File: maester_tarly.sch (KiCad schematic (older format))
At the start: 30 parts, among them J101 Micro_SD_Card_Det, J102 USB_B_Micro, J103 USB_A, J104 Conn_01x06, J105 Conn_01x10, J106 RJ45_Amphenol_RJMG1BD3B8K1ANR, J107 DF40GB(1.5)-48DS-0.4V, J108 DF40GB(1.5)-48DS-0.4V, J109 DF40GB(1.5)-48DS-0.4V, J110 DF40GB(1.5)-48DS-0.4V

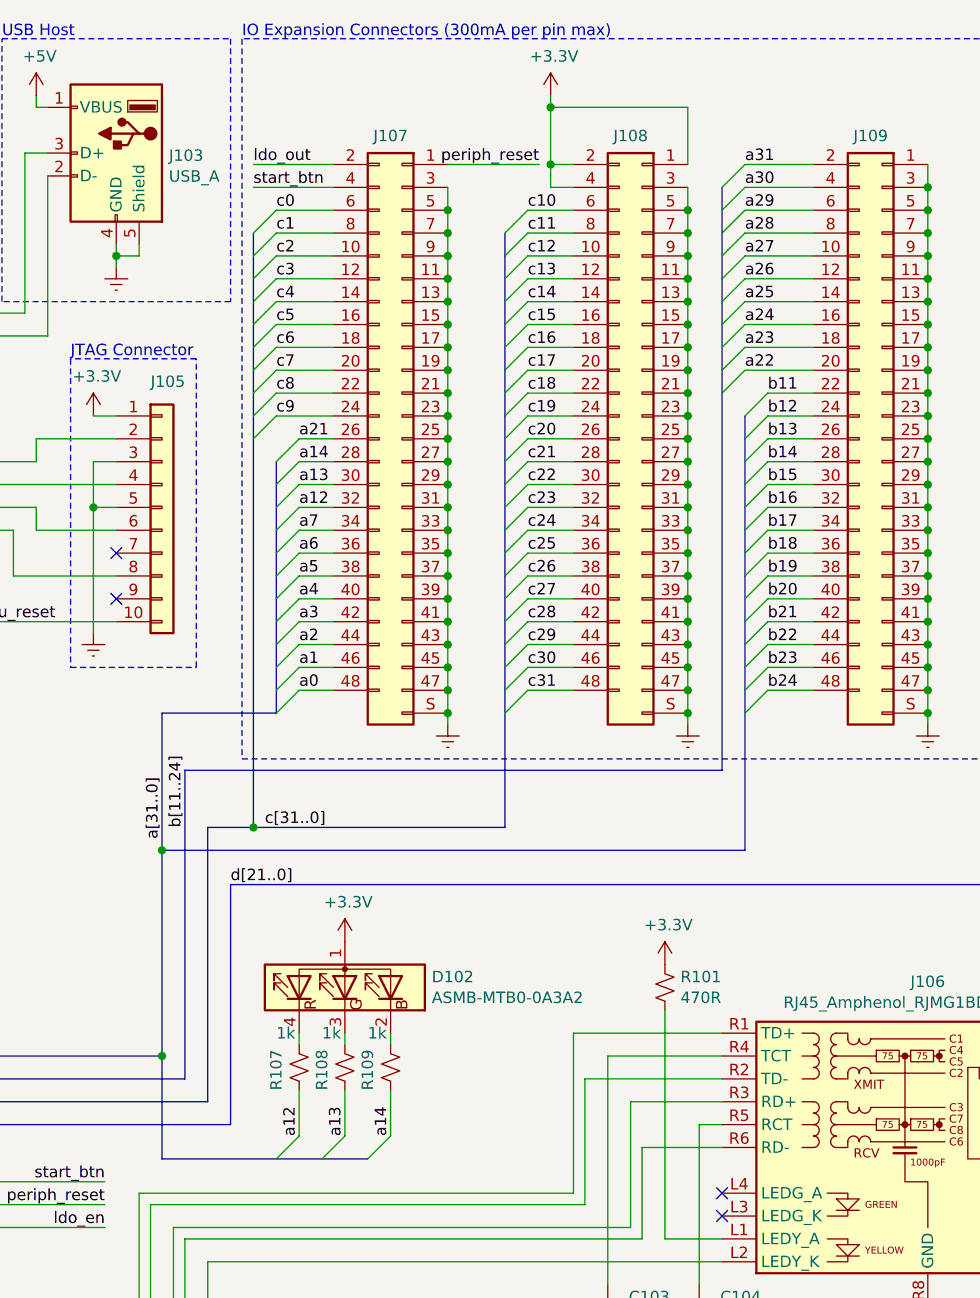
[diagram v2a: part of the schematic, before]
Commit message: Wired up J107 and J109
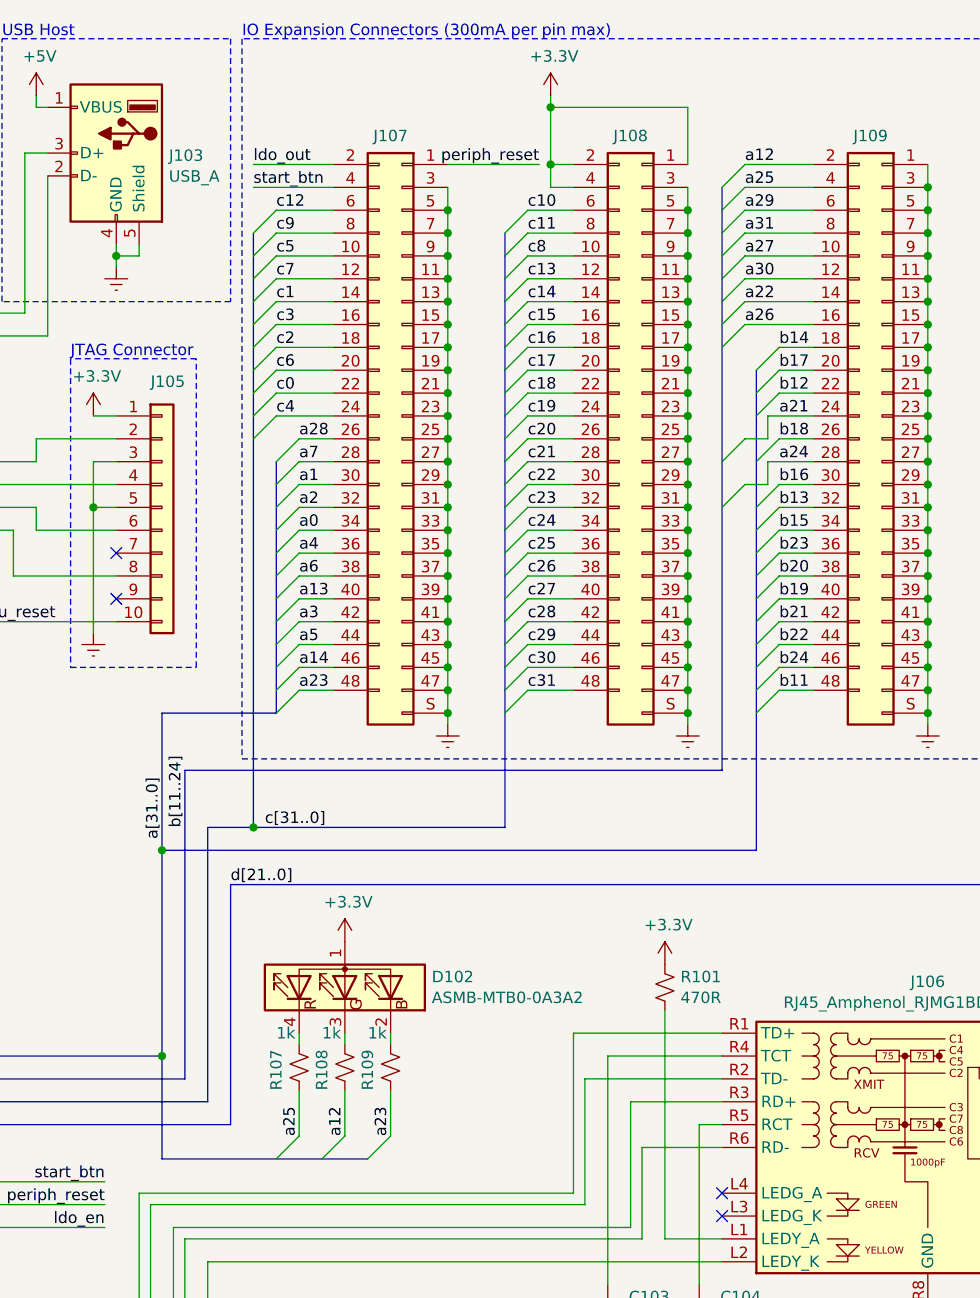
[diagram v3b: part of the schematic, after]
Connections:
- net a0: now also J107.34 (Pin_34); no longer J107.48 (Pin_48)
- net a1: now also J107.30 (Pin_30); no longer J107.46 (Pin_46)
- net a12: now also J109.2 (Pin_2), R108.2; no longer J107.32 (Pin_32), R107.2
- net a13: now also J107.40 (Pin_40); no longer J107.30 (Pin_30), R108.2
- net a14: now also J107.46 (Pin_46); no longer J107.28 (Pin_28), R109.2
- net a2: now also J107.32 (Pin_32); no longer J107.44 (Pin_44)
- net a21: now also J109.24 (Pin_24); no longer J107.26 (Pin_26)
- net a22: now also J109.14 (Pin_14); no longer J109.20 (Pin_20)
- net a23: now also J107.48 (Pin_48), R109.2; no longer J109.18 (Pin_18)
- net a24: now also J109.28 (Pin_28); no longer J109.16 (Pin_16)
- net a25: now also J109.4 (Pin_4), R107.2; no longer J109.14 (Pin_14)
- net a26: now also J109.16 (Pin_16); no longer J109.12 (Pin_12)
- net a28: now also J107.26 (Pin_26); no longer J109.8 (Pin_8)
- net a30: now also J109.12 (Pin_12); no longer J109.4 (Pin_4)
- net a31: now also J109.8 (Pin_8); no longer J109.2 (Pin_2)
- net a4: now also J107.36 (Pin_36); no longer J107.40 (Pin_40)
- net a5: now also J107.44 (Pin_44); no longer J107.38 (Pin_38)
- net a6: now also J107.38 (Pin_38); no longer J107.36 (Pin_36)
- net a7: now also J107.28 (Pin_28); no longer J107.34 (Pin_34)
- net b11: now also J109.48 (Pin_48); no longer J109.22 (Pin_22)
- net b12: now also J109.22 (Pin_22); no longer J109.24 (Pin_24)
- net b13: now also J109.32 (Pin_32); no longer J109.26 (Pin_26)
- net b14: now also J109.18 (Pin_18); no longer J109.28 (Pin_28)
- net b15: now also J109.34 (Pin_34); no longer J109.30 (Pin_30)
- net b16: now also J109.30 (Pin_30); no longer J109.32 (Pin_32)
- net b17: now also J109.20 (Pin_20); no longer J109.34 (Pin_34)
- net b18: now also J109.26 (Pin_26); no longer J109.36 (Pin_36)
- net b19: now also J109.40 (Pin_40); no longer J109.38 (Pin_38)
- net b20: now also J109.38 (Pin_38); no longer J109.40 (Pin_40)
- net b23: now also J109.36 (Pin_36); no longer J109.46 (Pin_46)
- net b24: now also J109.46 (Pin_46); no longer J109.48 (Pin_48)
- net c0: now also J107.22 (Pin_22); no longer J107.6 (Pin_6)
- net c1: now also J107.14 (Pin_14); no longer J107.8 (Pin_8)
- net c12: now also J107.6 (Pin_6); no longer J108.10 (Pin_10)
- net c2: now also J107.18 (Pin_18); no longer J107.10 (Pin_10)
- net c3: now also J107.16 (Pin_16); no longer J107.12 (Pin_12)
- net c4: now also J107.24 (Pin_24); no longer J107.14 (Pin_14)
- net c5: now also J107.10 (Pin_10); no longer J107.16 (Pin_16)
- net c6: now also J107.20 (Pin_20); no longer J107.18 (Pin_18)
- net c7: now also J107.12 (Pin_12); no longer J107.20 (Pin_20)
- net c8: now also J108.10 (Pin_10); no longer J107.22 (Pin_22)
- net c9: now also J107.8 (Pin_8); no longer J107.24 (Pin_24)

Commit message: 27 Unrouted traces remaiin.
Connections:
- net c10: now also J108.36 (Pin_36); no longer J108.6 (Pin_6)
- net c11: now also J108.48 (Pin_48); no longer J108.8 (Pin_8)
- net c13: now also J108.30 (Pin_30); no longer J108.12 (Pin_12)
- net c14: now also J108.46 (Pin_46); no longer J108.14 (Pin_14)
- net c15: now also J108.34 (Pin_34); no longer J108.16 (Pin_16)
- net c16: now also J108.44 (Pin_44); no longer J108.18 (Pin_18)
- net c17: now also J108.18 (Pin_18); no longer J108.20 (Pin_20)
- net c18: now also J108.42 (Pin_42); no longer J108.22 (Pin_22)
- net c19: now also J108.28 (Pin_28); no longer J108.24 (Pin_24)
- net c20: now also J108.24 (Pin_24); no longer J108.26 (Pin_26)
- net c21: now also J108.20 (Pin_20); no longer J108.28 (Pin_28)
- net c22: now also J108.38 (Pin_38); no longer J108.30 (Pin_30)
- net c23: now also J108.10 (Pin_10); no longer J108.32 (Pin_32)
- net c24: now also J108.32 (Pin_32); no longer J108.34 (Pin_34)
- net c25: now also J108.14 (Pin_14); no longer J108.36 (Pin_36)
- net c26: now also J108.26 (Pin_26); no longer J108.38 (Pin_38)
- net c27: now also J108.16 (Pin_16); no longer J108.40 (Pin_40)
- net c28: now also J108.12 (Pin_12); no longer J108.42 (Pin_42)
- net c29: now also J108.8 (Pin_8); no longer J108.44 (Pin_44)
- net c30: now also J108.40 (Pin_40); no longer J108.46 (Pin_46)
- net c31: now also J108.6 (Pin_6); no longer J108.48 (Pin_48)
- net c8: now also J108.22 (Pin_22); no longer J108.10 (Pin_10)
- net d0: now also J110.48 (Pin_48); no longer J110.6 (Pin_6)
- net d1: now also J110.46 (Pin_46); no longer J110.8 (Pin_8)
- net d10: now also J110.24 (Pin_24); no longer J110.26 (Pin_26)
- net d11: now also J110.10 (Pin_10); no longer J110.28 (Pin_28)
- net d12: now also J110.26 (Pin_26); no longer J110.30 (Pin_30)
- net d13: now also J110.22 (Pin_22); no longer J110.32 (Pin_32)
- net d14: now also J110.12 (Pin_12); no longer J110.34 (Pin_34)
- net d15: now also J110.30 (Pin_30); no longer J110.36 (Pin_36)
- net d16: now also J110.44 (Pin_44); no longer J110.38 (Pin_38)
- net d17: now also J110.34 (Pin_34); no longer J110.40 (Pin_40)
- net d18: now also J110.8 (Pin_8); no longer J110.42 (Pin_42)
- net d19: now also J110.38 (Pin_38); no longer J110.44 (Pin_44)
- net d2: now also J110.40 (Pin_40); no longer J110.10 (Pin_10)
- net d20: now also J110.14 (Pin_14); no longer J110.46 (Pin_46)
- net d21: now also J110.32 (Pin_32); no longer J110.48 (Pin_48)
- net d3: now also J110.36 (Pin_36); no longer J110.12 (Pin_12)
- net d4: now also J110.42 (Pin_42); no longer J110.14 (Pin_14)
- net d7: now also J110.28 (Pin_28); no longer J110.20 (Pin_20)
- net d8: now also J110.20 (Pin_20); no longer J110.22 (Pin_22)
- net d9: now also J110.6 (Pin_6); no longer J110.24 (Pin_24)
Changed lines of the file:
@@
 Text Label 7200 1700 0    50   ~ 0
 c7
-Text Label 8300 1600 0    50   ~ 0
+Text Label 8300 2200 0    50   ~ 0
 c8
 Text Label 7200 1500 0    50   ~ 0
 c9
-Text Label 8300 1400 0    50   ~ 0
+Text Label 8300 2900 0    50   ~ 0
 c10
-Text Label 8300 1500 0    50   ~ 0
+Text Label 8300 3500 0    50   ~ 0
 c11
 Text Label 7200 1400 0    50   ~ 0
 c12
-Text Label 8300 1700 0    50   ~ 0
+Text Label 8300 2600 0    50   ~ 0
 c13
-Text Label 8300 1800 0    50   ~ 0
+Text Label 8300 3400 0    50   ~ 0
 c14
-Text Label 8300 1900 0    50   ~ 0
+Text Label 8300 2800 0    50   ~ 0
 c15
+Text Label 8300 3300 0    50   ~ 0
+c16
 Text Label 8300 2000 0    50   ~ 0
-c16
+c17
+Text Label 8300 3200 0    50   ~ 0
+c18
+Text Label 8300 2500 0    50   ~ 0
+c19
+Text Label 8300 2300 0    50   ~ 0
+c20
 Text Label 8300 2100 0    50   ~ 0
-c17
-Text Label 8300 2200 0    50   ~ 0
-c18
-Text Label 8300 2300 0    50   ~ 0
-c19
-Text Label 8300 2400 0    50   ~ 0
-c20
-Text Label 8300 2500 0    50   ~ 0
 c21
 Wire Wire Line
@@
 Wire Wire Line
 	1250 2300 4250 2300
-Text Label 10400 1400 0    50   ~ 0
+Text Label 10400 3500 0    50   ~ 0
 d0
-Text Label 10400 1500 0    50   ~ 0
+Text Label 10400 3400 0    50   ~ 0
 d1
-Text Label 10400 1600 0    50   ~ 0
+Text Label 10400 3100 0    50   ~ 0
 d2
-Text Label 10400 1700 0    50   ~ 0
+Text Label 10400 2900 0    50   ~ 0
 d3
-Text Label 10400 1800 0    50   ~ 0
+Text Label 10400 3200 0    50   ~ 0
 d4
 Text Label 10400 1900 0    50   ~ 0
@@
 Text Label 10400 2000 0    50   ~ 0
 d6
+Text Label 10400 2500 0    50   ~ 0
+d7
 Text Label 10400 2100 0    50   ~ 0
-d7
+d8
+Text Label 10400 1400 0    50   ~ 0
+d9
+Text Label 10400 2300 0    50   ~ 0
+d10
+Text Label 10400 1600 0    50   ~ 0
+d11
+Text Label 10400 2400 0    50   ~ 0
+d12
 Text Label 10400 2200 0    50   ~ 0
-d8
-Text Label 10400 2300 0    50   ~ 0
-d9
-Text Label 10400 2400 0    50   ~ 0
-d10
-Text Label 10400 2500 0    50   ~ 0
-d11
+d13
+Text Label 10400 1700 0    50   ~ 0
+d14
 Text Label 10400 2600 0    50   ~ 0
-d12
+d15
+Text Label 10400 3300 0    50   ~ 0
+d16
+Text Label 10400 2800 0    50   ~ 0
+d17
+Text Label 10400 1500 0    50   ~ 0
+d18
+Text Label 10400 3000 0    50   ~ 0
+d19
+Text Label 10400 1800 0    50   ~ 0
+d20
 Text Label 10400 2700 0    50   ~ 0
-d13
-Text Label 10400 2800 0    50   ~ 0
-d14
-Text Label 10400 2900 0    50   ~ 0
-d15
-Text Label 10400 3000 0    50   ~ 0
-d16
-Text Label 10400 3100 0    50   ~ 0
-d17
-Text Label 10400 3200 0    50   ~ 0
-d18
-Text Label 10400 3300 0    50   ~ 0
-d19
-Text Label 10400 3400 0    50   ~ 0
-d20
-Text Label 10400 3500 0    50   ~ 0
 d21
 Wire Wire Line
@@
 	8400 900  8400 950
 Wire Wire Line
+	10600 3100 10400 3100
+Wire Wire Line
+	10600 2600 10400 2600
+Wire Wire Line
 	10600 1400 10400 1400
 Wire Wire Line
@@
 	10600 2500 10400 2500
 Wire Wire Line
-	10600 2600 10400 2600
-Wire Wire Line
 	10600 2700 10400 2700
 Wire Wire Line
@@
 	10600 3000 10400 3000
 Wire Wire Line
-	10600 3100 10400 3100
-Wire Wire Line
 	10600 3200 10400 3200
 Wire Wire Line
@@
 	8200 2600 8300 2500
 Entry Wire Line
+	10300 3200 10400 3100
+Entry Wire Line
+	10300 2700 10400 2600
+Entry Wire Line
 	10300 1500 10400 1400
 Entry Wire Line
@@
 	10300 2600 10400 2500
 Entry Wire Line
-	10300 2700 10400 2600
-Entry Wire Line
 	10300 2800 10400 2700
 Entry Wire Line
@@
 Entry Wire Line
 	10300 3100 10400 3000
-Entry Wire Line
-	10300 3200 10400 3100
 Entry Wire Line
 	10300 3300 10400 3200
@@
 Entry Wire Line
 	8200 2700 8300 2600
-Text Label 8300 3500 0    50   ~ 0
+Text Label 8300 1400 0    50   ~ 0
 c31
-Text Label 8300 3400 0    50   ~ 0
+Text Label 8300 3100 0    50   ~ 0
 c30
-Text Label 8300 3300 0    50   ~ 0
+Text Label 8300 1500 0    50   ~ 0
 c29
-Text Label 8300 3200 0    50   ~ 0
+Text Label 8300 1700 0    50   ~ 0
 c28
-Text Label 8300 3100 0    50   ~ 0
+Text Label 8300 1900 0    50   ~ 0
 c27
+Text Label 8300 2400 0    50   ~ 0
+c26
+Text Label 8300 1800 0    50   ~ 0
+c25
+Text Label 8300 2700 0    50   ~ 0
+c24
+Text Label 8300 1600 0    50   ~ 0
+c23
 Text Label 8300 3000 0    50   ~ 0
-c26
-Text Label 8300 2900 0    50   ~ 0
-c25
-Text Label 8300 2800 0    50   ~ 0
-c24
-Text Label 8300 2700 0    50   ~ 0
-c23
-Text Label 8300 2600 0    50   ~ 0
 c22
 Wire Wire Line
